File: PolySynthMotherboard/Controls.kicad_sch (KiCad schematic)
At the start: 101 parts, among them SW601 ENV1_B, SW602 ENV2_B, SW603 LFO1_B, SW604 LFO2_B, SW605 LFO3_B, SW606 MIX1_B, SW607 MIX2_B, SW608 ALT_B, SW609 FF_B, SW610 HP_B, SW611 HP_B, SW612 ENC_MENU, U204 ILI9341, U501 MCP23S17_SS

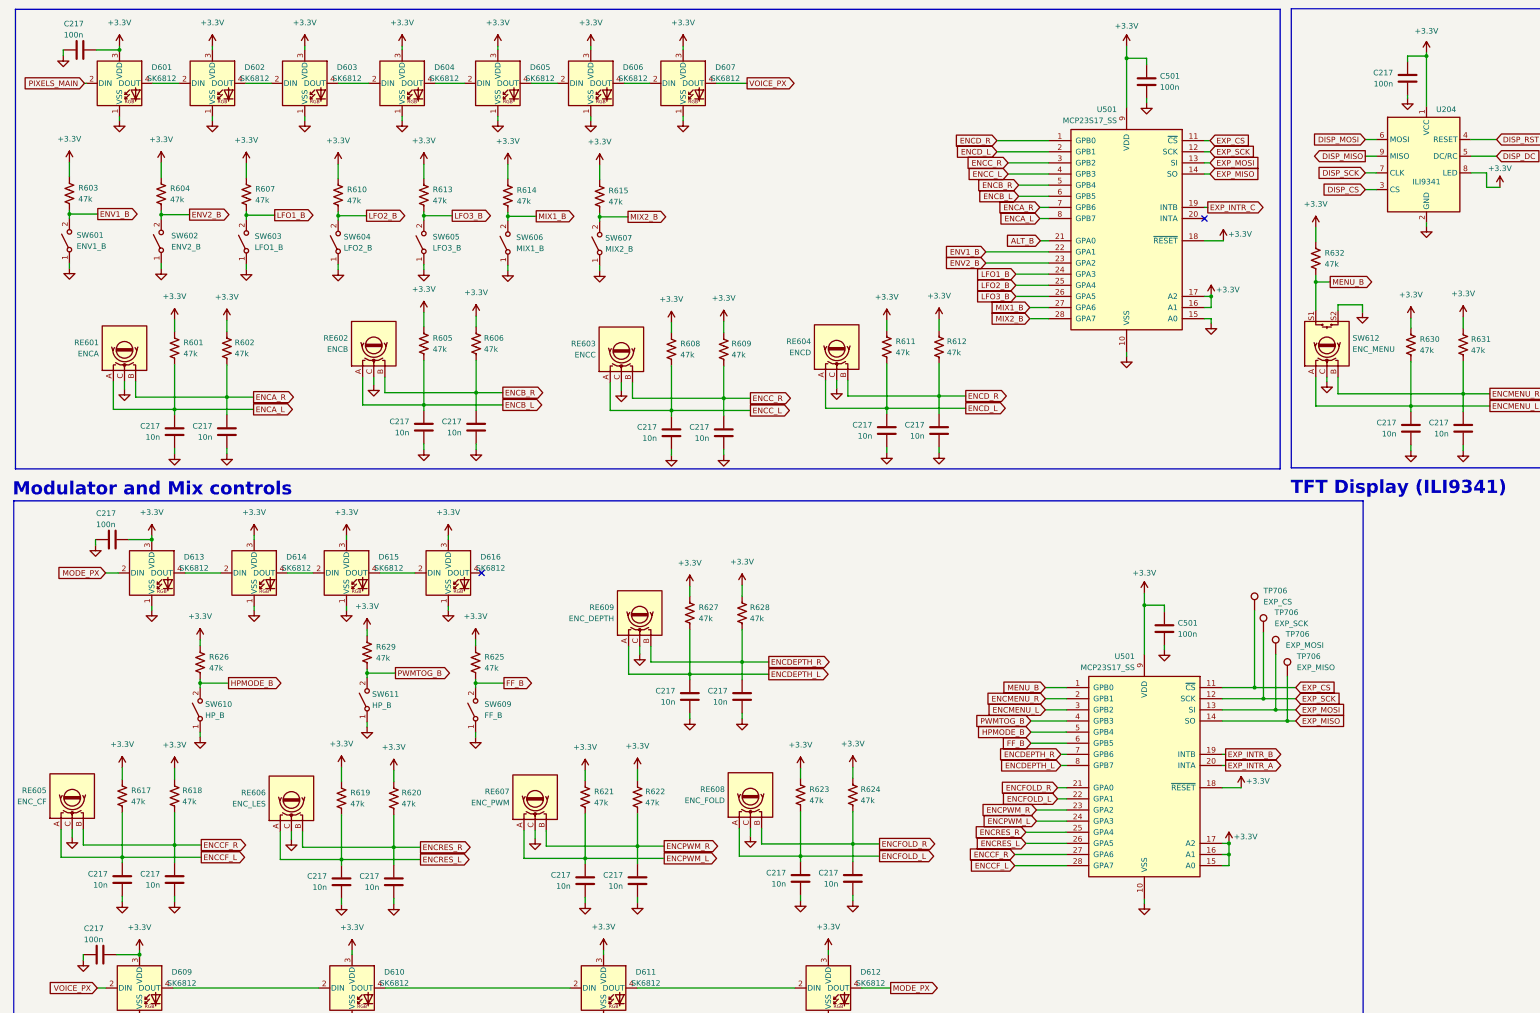
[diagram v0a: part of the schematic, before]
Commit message: updated to kicad 8
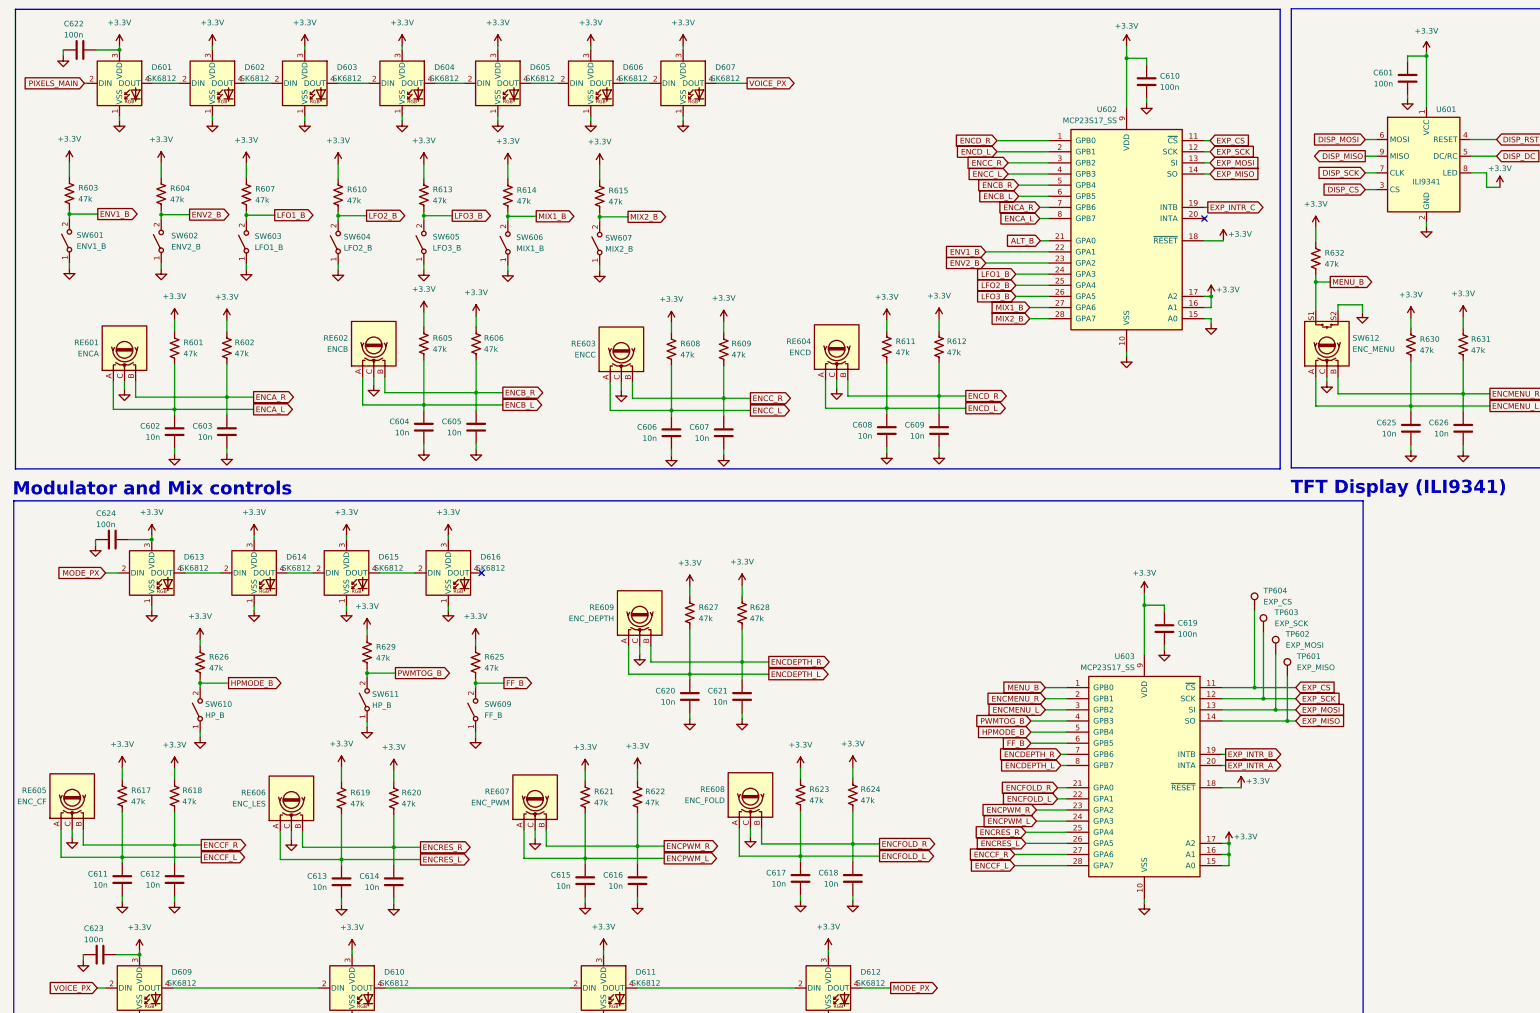
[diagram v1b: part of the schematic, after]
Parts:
- renumbered C217 to C601, C217 to C602, C217 to C603, C217 to C604, C217 to C605, C217 to C606, C217 to C607, C217 to C608, C217 to C609, C501 to C610, C217 to C611, C217 to C612, C217 to C613, C217 to C614, C217 to C615, C217 to C616, C217 to C617, C217 to C618, C501 to C619, C217 to C620, C217 to C621, C217 to C622, C217 to C623, C217 to C624, C217 to C625, C217 to C626, TP706 to TP601, TP706 to TP602, TP706 to TP603, TP706 to TP604, U204 to U601, U501 to U602, U501 to U603

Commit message: fixed footprints, switched optocoupler
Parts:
- R601, R602, R603, R604, R605, R606, R607, R608, R609, R610, R611, R612, R613, R614, R615, R616, R617, R618, R619, R620, R621, R622, R623, R624, R625, R626, R627, R628, R629, R630, R631, R632: footprint PCM_Resistor_SMD_AKL:R_0805_2012Metric -> Resistor_SMD:R_0805_2012Metric
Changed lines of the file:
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@@
 			)
 		)
-		(property "Footprint" "PCM_Resistor_SMD_AKL:R_0805_2012Metric"
+		(property "Footprint" "Resistor_SMD:R_0805_2012Metric"
 			(at 214.757 93.726 90)
 			(effects
@@
 			)
 		)
-		(property "Footprint" "PCM_Resistor_SMD_AKL:R_0805_2012Metric"
+		(property "Footprint" "Resistor_SMD:R_0805_2012Metric"
 			(at 346.329 93.218 90)
 			(effects
@@
 			)
 		)
-		(property "Footprint" "PCM_Resistor_SMD_AKL:R_0805_2012Metric"
+		(property "Footprint" "Resistor_SMD:R_0805_2012Metric"
 			(at 121.031 92.964 90)
 			(effects
@@
 			)
 		)
-		(property "Footprint" "PCM_Resistor_SMD_AKL:R_0805_2012Metric"
+		(property "Footprint" "Resistor_SMD:R_0805_2012Metric"
 			(at 195.072 195.961 90)
 			(effects
@@
 			)
 		)
-		(property "Footprint" "PCM_Resistor_SMD_AKL:R_0805_2012Metric"
+		(property "Footprint" "Resistor_SMD:R_0805_2012Metric"
 			(at 102.235 196.723 90)
 			(effects
@@
 			)
 		)
-		(property "Footprint" "PCM_Resistor_SMD_AKL:R_0805_2012Metric"
+		(property "Footprint" "Resistor_SMD:R_0805_2012Metric"
 			(at 89.535 59.055 90)
 			(effects
@@
 			)
 		)
-		(property "Footprint" "PCM_Resistor_SMD_AKL:R_0805_2012Metric"
+		(property "Footprint" "Resistor_SMD:R_0805_2012Metric"
 			(at 128.27 59.182 90)
 			(effects
@@
 			)
 		)
-		(property "Footprint" "PCM_Resistor_SMD_AKL:R_0805_2012Metric"
+		(property "Footprint" "Resistor_SMD:R_0805_2012Metric"
 			(at 90.297 196.723 90)
 			(effects
@@
 			)
 		)
-		(property "Footprint" "PCM_Resistor_SMD_AKL:R_0805_2012Metric"
+		(property "Footprint" "Resistor_SMD:R_0805_2012Metric"
 			(at 377.19 81.915 90)
 			(effects
@@
 			)
 		)
-		(property "Footprint" "PCM_Resistor_SMD_AKL:R_0805_2012Metric"
+		(property "Footprint" "Resistor_SMD:R_0805_2012Metric"
 			(at 120.904 165.735 90)
 			(effects
@@
 			)
 		)
-		(property "Footprint" "PCM_Resistor_SMD_AKL:R_0805_2012Metric"
+		(property "Footprint" "Resistor_SMD:R_0805_2012Metric"
 			(at 52.197 93.98 90)
 			(effects
@@
 			)
 		)
-		(property "Footprint" "PCM_Resistor_SMD_AKL:R_0805_2012Metric"
+		(property "Footprint" "Resistor_SMD:R_0805_2012Metric"
 			(at 145.923 196.469 90)
 			(effects
@@
 			)
 		)
-		(property "Footprint" "PCM_Resistor_SMD_AKL:R_0805_2012Metric"
+		(property "Footprint" "Resistor_SMD:R_0805_2012Metric"
 			(at 49.149 58.801 90)
 			(effects
@@
 			)
 		)
-		(property "Footprint" "PCM_Resistor_SMD_AKL:R_0805_2012Metric"
+		(property "Footprint" "Resistor_SMD:R_0805_2012Metric"
 			(at 149.225 59.309 90)
 			(effects
@@
 			)
 		)
-		(property "Footprint" "PCM_Resistor_SMD_AKL:R_0805_2012Metric"
+		(property "Footprint" "Resistor_SMD:R_0805_2012Metric"
 			(at 177.546 94.234 90)
 			(effects
@@
 			)
 		)
-		(property "Footprint" "PCM_Resistor_SMD_AKL:R_0805_2012Metric"
+		(property "Footprint" "Resistor_SMD:R_0805_2012Metric"
 			(at 169.799 154.432 90)
 			(effects
@@
 			)
 		)
-		(property "Footprint" "PCM_Resistor_SMD_AKL:R_0805_2012Metric"
+		(property "Footprint" "Resistor_SMD:R_0805_2012Metric"
 			(at 68.58 58.928 90)
 			(effects
@@
 			)
 		)
-		(property "Footprint" "PCM_Resistor_SMD_AKL:R_0805_2012Metric"
+		(property "Footprint" "Resistor_SMD:R_0805_2012Metric"
 			(at 207.01 195.961 90)
 			(effects
@@
 			)
 		)
-		(property "Footprint" "PCM_Resistor_SMD_AKL:R_0805_2012Metric"
+		(property "Footprint" "Resistor_SMD:R_0805_2012Metric"
 			(at 40.259 196.215 90)
 			(effects
@@
 			)
 		)
-		(property "Footprint" "PCM_Resistor_SMD_AKL:R_0805_2012Metric"
+		(property "Footprint" "Resistor_SMD:R_0805_2012Metric"
 			(at 64.135 93.98 90)
 			(effects
@@
 			)
 		)
-		(property "Footprint" "PCM_Resistor_SMD_AKL:R_0805_2012Metric"
+		(property "Footprint" "Resistor_SMD:R_0805_2012Metric"
 			(at 312.674 73.533 90)
 			(effects
@@
 			)
 		)
-		(property "Footprint" "PCM_Resistor_SMD_AKL:R_0805_2012Metric"
+		(property "Footprint" "Resistor_SMD:R_0805_2012Metric"
 			(at 109.093 92.964 90)
 			(effects
@@
 			)
 		)
-		(property "Footprint" "PCM_Resistor_SMD_AKL:R_0805_2012Metric"
+		(property "Footprint" "Resistor_SMD:R_0805_2012Metric"
 			(at 96.139 163.449 90)
 			(effects
@@
 			)
 		)
-		(property "Footprint" "PCM_Resistor_SMD_AKL:R_0805_2012Metric"
+		(property "Footprint" "Resistor_SMD:R_0805_2012Metric"
 			(at 334.391 93.218 90)
 			(effects
@@
 			)
 		)
-		(property "Footprint" "PCM_Resistor_SMD_AKL:R_0805_2012Metric"
+		(property "Footprint" "Resistor_SMD:R_0805_2012Metric"
 			(at 226.695 93.726 90)
 			(effects
@@
 			)
 		)
-		(property "Footprint" "PCM_Resistor_SMD_AKL:R_0805_2012Metric"
+		(property "Footprint" "Resistor_SMD:R_0805_2012Metric"
 			(at 52.197 196.215 90)
 			(effects
@@
 			)
 		)
-		(property "Footprint" "PCM_Resistor_SMD_AKL:R_0805_2012Metric"
+		(property "Footprint" "Resistor_SMD:R_0805_2012Metric"
 			(at 157.861 196.469 90)
 			(effects
@@
 			)
 		)
-		(property "Footprint" "PCM_Resistor_SMD_AKL:R_0805_2012Metric"
+		(property "Footprint" "Resistor_SMD:R_0805_2012Metric"
 			(at 28.194 58.674 90)
 			(effects
@@
 			)
 		)
-		(property "Footprint" "PCM_Resistor_SMD_AKL:R_0805_2012Metric"
+		(property "Footprint" "Resistor_SMD:R_0805_2012Metric"
 			(at 181.737 154.432 90)
 			(effects
@@
 			)
 		)
-		(property "Footprint" "PCM_Resistor_SMD_AKL:R_0805_2012Metric"
+		(property "Footprint" "Resistor_SMD:R_0805_2012Metric"
 			(at 165.608 94.234 90)
 			(effects
@@
 			)
 		)
-		(property "Footprint" "PCM_Resistor_SMD_AKL:R_0805_2012Metric"
+		(property "Footprint" "Resistor_SMD:R_0805_2012Metric"
 			(at 109.093 59.055 90)
 			(effects
@@
 			)
 		)
-		(property "Footprint" "PCM_Resistor_SMD_AKL:R_0805_2012Metric"
+		(property "Footprint" "Resistor_SMD:R_0805_2012Metric"
 			(at 58.039 165.735 90)
 			(effects

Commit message: added terminations
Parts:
- added R633, R634, R635, R636, R637, R638: 22R, symbol Device:R_US
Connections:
- net DISP_MISO: now also R638.1; no longer U601.9 (MISO)
- net EXP_INTR_A: now also R637.2; no longer U603.20 (INTA)
- net EXP_INTR_B: now also R636.2; no longer U603.19 (INTB)
- net EXP_INTR_C: now also R634.2; no longer U602.19 (INTB)
- net EXP_MISO: now also R633.2, R635.2; no longer TP601.1, U602.14 (SO), U603.14 (SO)
- new net: R633.1, U602.14 (SO)
- new net: R634.1, U602.19 (INTB)
- new net: R638.2, U601.9 (MISO)
- new net: R635.1, TP601.1, U603.14 (SO)
- new net: R636.1, U603.19 (INTB)
- new net: R637.1, U603.20 (INTA)
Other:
- moved on the sheet: C601, C604, C605, C606, C607, C608, C609, C610, R605, R606, R608, R609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

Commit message: board iteration
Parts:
- removed TP601: EXP_MISO, TestPoint:TestPoint_Pad_D1.0mm_Value, symbol Connector:TestPoint
- removed TP602: EXP_MOSI, TestPoint:TestPoint_Pad_D1.0mm_Value, symbol Connector:TestPoint
- removed TP603: EXP_SCK, TestPoint:TestPoint_Pad_D1.0mm_Value, symbol Connector:TestPoint
- removed TP604: EXP_CS, TestPoint:TestPoint_Pad_D1.0mm_Value, symbol Connector:TestPoint
- added R639: 47k, Resistor_SMD:R_0805_2012Metric, symbol Device:R_US
- R633, R634, R635, R636, R637, R638: footprint (none) -> Resistor_SMD:R_0805_2012Metric
- SW612: footprint Alps_Rotary_Encoder:RotaryEncoder_Alps_EC11E-Switch_Vertical_H20mm_5Pin -> Rotary_Encoder:RotaryEncoder_Alps_EC11E-Switch_Vertical_H20mm_5Pin
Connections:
- net +3.3V: now also R639.1
- net DISP_CS: now also R639.2
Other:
- moved on the sheet: R638
